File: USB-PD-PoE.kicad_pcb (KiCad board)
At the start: 4 copper layers, 39.6 x 87.4 mm, 134 parts, among them J1 8P8C_Shielded, J2 8P8C_Shielded, J3 TagConnect_TC2030_SWD, J4 USB_C_Receptacle_USB2.0, Q1 FDC2512, Q2 2N7002, Q3 2N7002, Q4 2N7002, Q5 APM4953KC, Q6 2N7002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

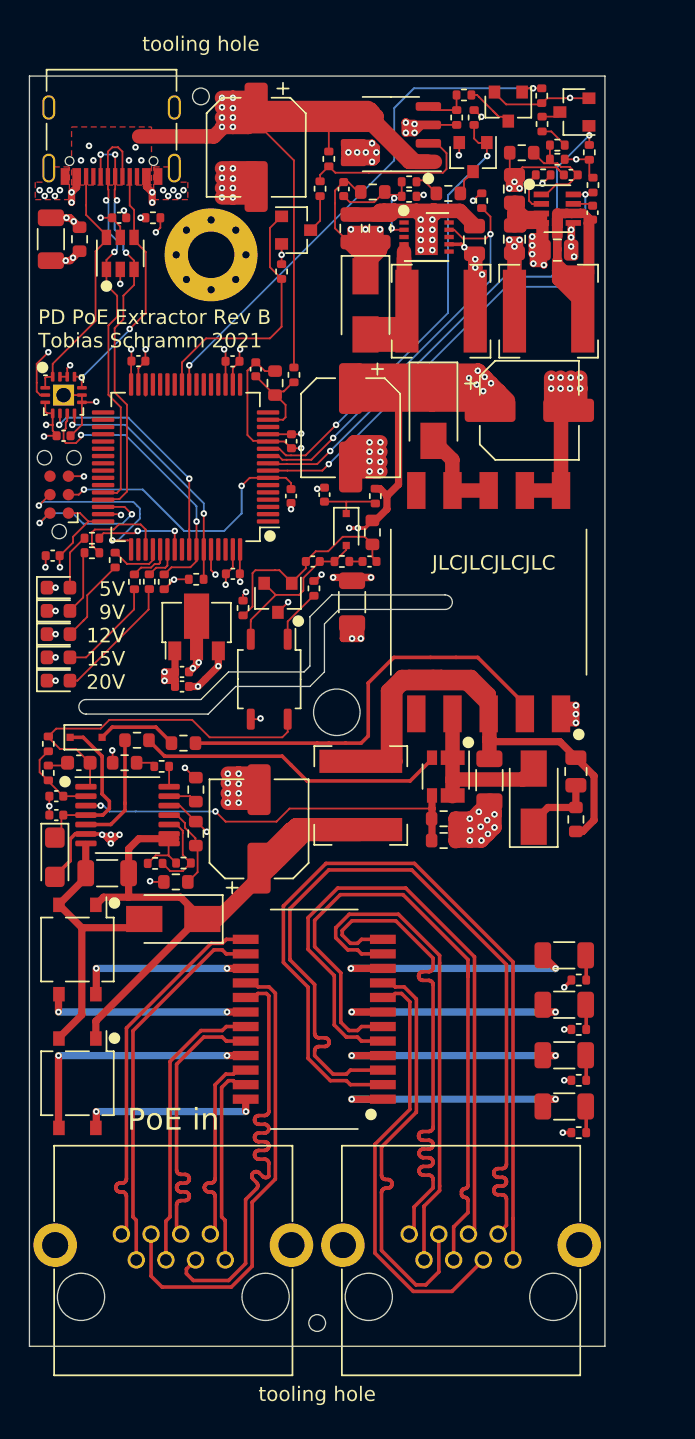
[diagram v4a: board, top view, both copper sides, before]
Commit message: Optimize design for manufacturing
Replace components not available at JLC anymore.
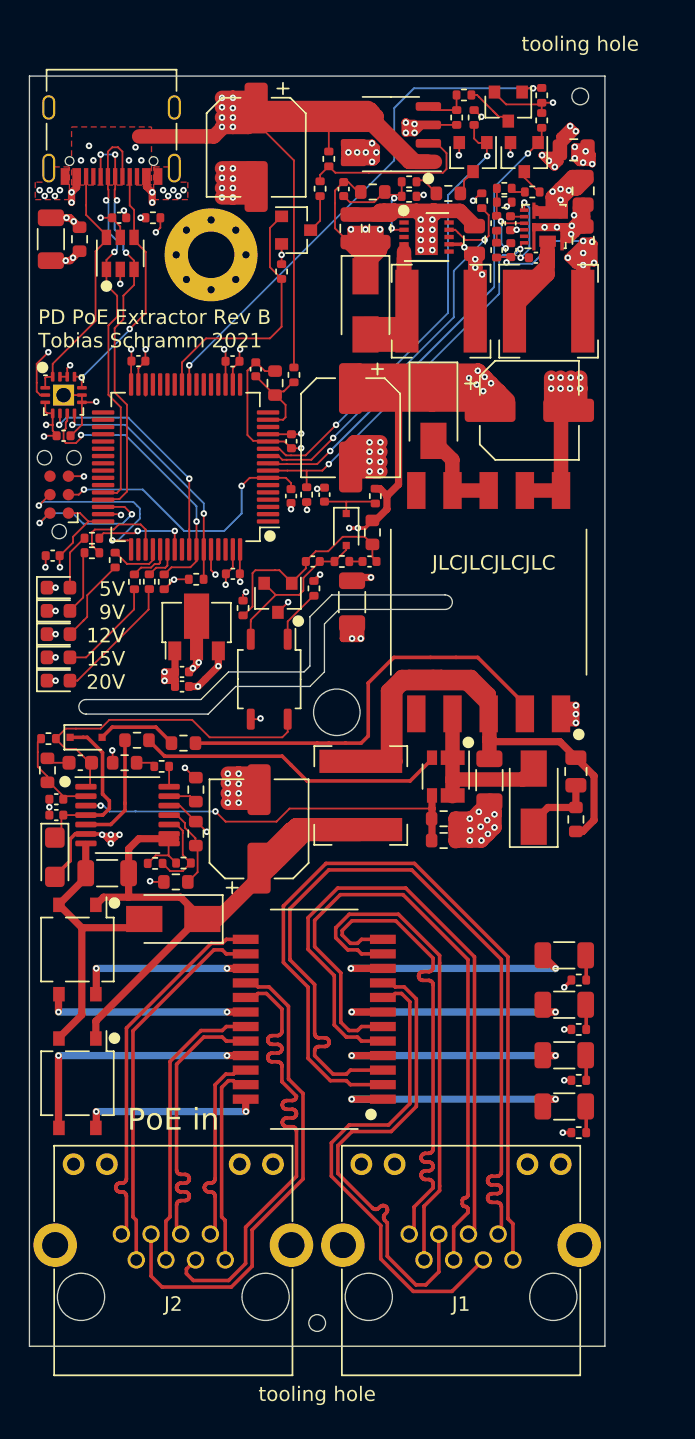
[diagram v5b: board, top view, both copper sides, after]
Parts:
- removed U8: SY8303, Package_TO_SOT_SMD:SOT-23-8
- added C41: 4.7uF, Capacitor_SMD:C_0402_1005Metric, F.Cu at (133.2, 76.1)
- added U10: SY8368, Package_QFN_Silergy:QFN_3x3-10_SY8368, F.Cu at (135.5, 76.3)
- J1, J2: footprint Connector_RJ_Ckmtw:Connector_8P8C_R-RJ45R08P-B000 -> Connector_RJ_Ckmtw:Connector_8P8C_R-RJ45R08P-C000
- R28: value 100kR -> 10kR
- R3: value 1.6kR -> 300R
- R31: value 110kR -> 100kR; footprint Resistor_SMD:R_0603_1608Metric -> Resistor_SMD:R_0402_1005Metric
- R6: value 4.3kR -> 5.6kR
- R9: value 402R -> 390R; footprint Resistor_SMD:R_0402_1005Metric -> Resistor_SMD:R_0603_1608Metric
- moved R27 29.0 mm to (119.2, 94.8), turned to 90 degrees
- moved H4 26.1 mm to (138.0, 67.4)
- moved C29 6.62 mm to (133.2, 78.0), turned to 90 degrees
- moved R28 6.08 mm to (132.2, 78.0), turned to 270 degrees
- moved R31 5.15 mm to (132.2, 76.1), turned to 270 degrees
- moved C28 4.98 mm to (134.9, 78.5), turned to 180 degrees
- moved C39 4.89 mm to (137.6, 71.1), turned to 180 degrees
- moved C31 4.73 mm to (138.2, 77.3)
- moved R36 4.72 mm to (134.7, 74.0), turned to 0 degrees
- moved R35 4.71 mm to (132.8, 73.7)
- moved R32 4.69 mm to (132.8, 74.7)
- moved Q3 4.64 mm to (134.2, 71.6), turned to 270 degrees
- moved C23 4.44 mm to (138.2, 73.9), turned to 90 degrees
- moved R33 3.95 mm to (135.3, 69.0), turned to 270 degrees
- moved R8 0.36 mm to (101.4, 111.6), turned to 180 degrees
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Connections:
- R28 pad 2: GND -> /BUCK_OUT
- R31 pad 1: /BUCK_OUT -> Net-(C29-Pad2)
- R31 pad 2: Net-(C29-Pad2) -> Net-(R28-Pad1)
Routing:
- net /BUCK_OUT: track 67.5 -> 97.8 mm, vias 12 -> 18
- net Net-(C28-Pad1): track 35.3 -> 12.7 mm
- net +12V: track 161.4 -> 170.4 mm
- net /BUCK_EN: track 34.2 -> 27.0 mm
- net /BOOST_OUT: track 59.4 -> 64.5 mm
- net GND: track 152.6 -> 147.8 mm, vias 81 -> 87
- net /9V_EN: track 37.0 -> 32.7 mm
- net /ETH_DEV2-: track 29.9 -> 34.0 mm
- net /ETH_DEV2+: track 29.9 -> 34.0 mm
- net Net-(C28-Pad2): track 1.38 -> 5.26 mm, vias 0 -> 2
- net Net-(R28-Pad1): track 2.94 -> 0.87 mm
- net /ETH_DEV1+: track 36.5 -> 34.5 mm
- net Net-(C29-Pad2): track 8.00 -> 6.42 mm, vias 0 -> 2
- net /ETH_POE2-: track 32.5 -> 34.1 mm
- net /ETH_POE2+: track 32.5 -> 34.1 mm
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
